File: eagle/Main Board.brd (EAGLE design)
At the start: 101.6 x 53.3 mm, 3 parts

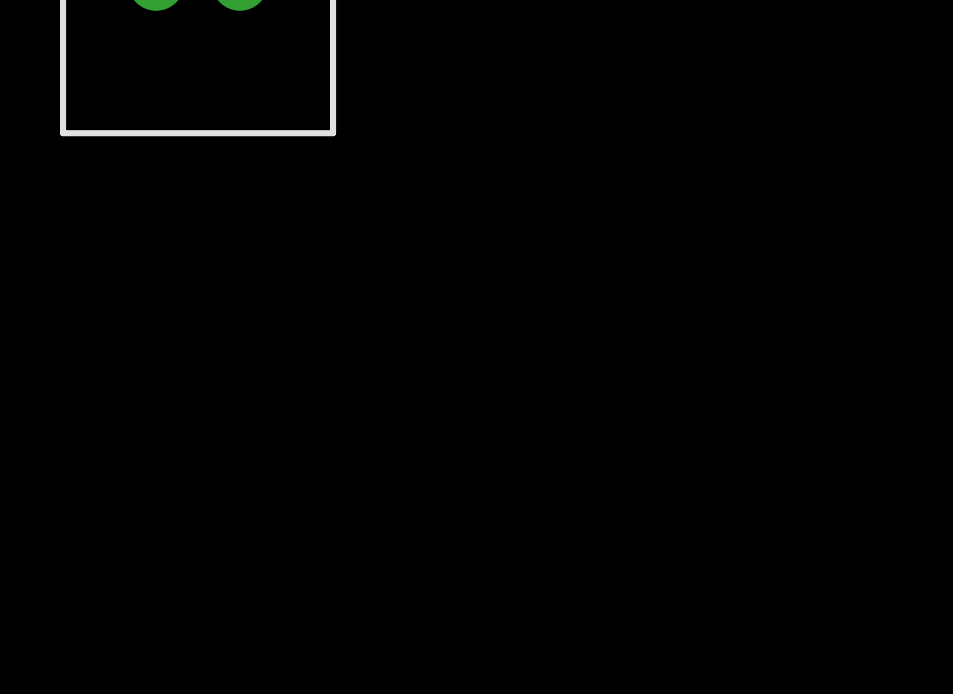
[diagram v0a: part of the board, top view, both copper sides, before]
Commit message: Wired rotary encoder to arduino.
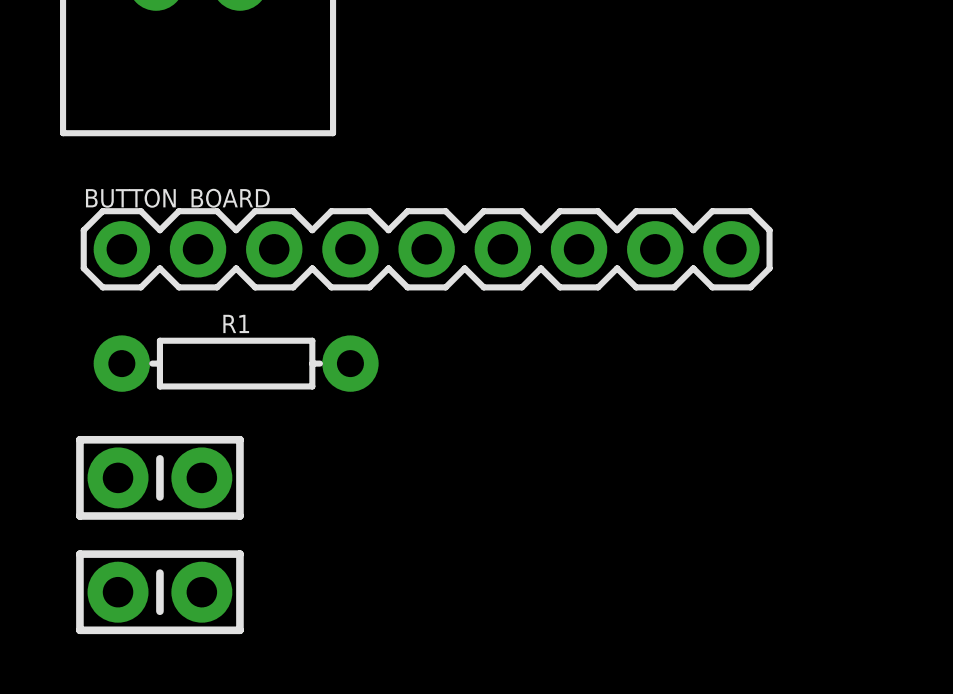
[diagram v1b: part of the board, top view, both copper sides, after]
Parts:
- added BUTTON_BOARD: (no value), SparkFun-Connectors:1X09
- added C1, C2: 0.1uF, SparkFun-Capacitors:CAP-PTH-SMALL-KIT
- added R1: 10k, SparkFun-Resistors:AXIAL-0.3
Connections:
- new net 5V: B1.5V, B1.5V@1, B1.5V@2, BUTTON_BOARD.1
- new net KEY: BUTTON_BOARD.3
- new net LED_B: B1.6, BUTTON_BOARD.9
- new net LED_G: B1.5, BUTTON_BOARD.8
- new net LED_R: B1.4, BUTTON_BOARD.7
- new net ROT_A: B1.2, BUTTON_BOARD.4, C1.2
- new net ROT_B: B1.7, BUTTON_BOARD.5, C2.2
- new net ROT_SW: B1.3, BUTTON_BOARD.6, R1.P$2
- net GND: now also B1.GND, B1.GND@1, B1.GND@2, B1.GND@3, B1.GND@4, BUTTON_BOARD.2, C1.1, C2.1, R1.P$1
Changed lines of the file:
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@@
 </element>
 <element name="J1" library="SparkFun-Connectors" package="2X8-SHROUDED_LOCK" value="" x="-106.68" y="12.7" smashed="yes"/>
+<element name="BUTTON_BOARD" library="SparkFun-Connectors" package="1X09" value="" x="-109.22" y="-5.08" smashed="yes">
+<attribute name="NAME" x="-110.49" y="-3.683" size="0.6096" layer="25" font="vector" ratio="20"/>
+<attribute name="VALUE" x="-110.49" y="-7.112" size="0.6096" layer="27" font="vector" ratio="20"/>
+</element>
+<element name="R1" library="SparkFun-Resistors" package="AXIAL-0.3" value="10k" x="-105.41" y="-8.89" smashed="yes">
+<attribute name="NAME" x="-105.41" y="-7.874" size="0.6096" layer="25" font="vector" ratio="20" align="bottom-center"/>
+<attribute name="PROD_ID" value="RES-12183" x="-105.41" y="-8.89" size="1.778" layer="27" display="off"/>
+<attribute name="VALUE" x="-105.41" y="-9.906" size="0.6096" layer="27" font="vector" ratio="20" align="top-center"/>
+</element>
+<element name="C1" library="SparkFun-Capacitors" package="CAP-PTH-SMALL-KIT" value="0.1uF" x="-107.95" y="-12.7" smashed="yes">
+<attribute name="PROD_ID" value="CAP-08370" x="-107.95" y="-12.7" size="1.778" layer="27" display="off"/>
+</element>
+<element name="C2" library="SparkFun-Capacitors" package="CAP-PTH-SMALL-KIT" value="0.1uF" x="-107.95" y="-16.51" smashed="yes">
+<attribute name="PROD_ID" value="CAP-08370" x="-107.95" y="-16.51" size="1.778" layer="27" display="off"/>
+</element>
 </elements>
 <signals>
@@
 <signal name="GND">
 <contactref element="J1" pad="4"/>
+<contactref element="B1" pad="GND@1"/>
+<contactref element="B1" pad="GND@3" route="any" routetag="B1.GND"/>
+<contactref element="B1" pad="GND@4" route="any" routetag="B1.GND"/>
+<contactref element="B1" pad="GND" route="any" routetag="B1.GND"/>
+<contactref element="C1" pad="1"/>
+<contactref element="C2" pad="1"/>
+<contactref element="BUTTON_BOARD" pad="2"/>
+<contactref element="B1" pad="GND@2"/>
+<contactref element="R1" pad="P$1"/>
+<wire x1="-109.347" y1="-12.7" x2="-109.347" y2="-16.51" width="0" layer="19" extent="1-1"/>
+<wire x1="-109.22" y1="-8.89" x2="-109.347" y2="-12.7" width="0" layer="19" extent="1-1"/>
+<wire x1="-106.68" y1="-5.08" x2="-109.22" y2="-8.89" width="0" layer="19" extent="1-1"/>
+<wire x1="-105.283" y1="19.05" x2="-106.68" y2="-5.08" width="0" layer="19" extent="1-1"/>
+<wire x1="26.67" y1="50.8" x2="-105.283" y2="19.05" width="0" layer="19" extent="1-1"/>
+<wire x1="93.98" y1="7.62" x2="96.52" y2="7.62" width="0" layer="19" extent="1-1"/>
+<wire x1="43.18" y1="2.54" x2="40.64" y2="2.54" width="0" layer="19" extent="1-1"/>
+</signal>
+<signal name="ROT_A">
+<contactref element="B1" pad="2"/>
+<contactref element="BUTTON_BOARD" pad="4"/>
+<contactref element="C1" pad="2"/>
+<wire x1="-101.6" y1="-5.08" x2="-106.553" y2="-12.7" width="0" layer="19" extent="1-1"/>
+<wire x1="58.42" y1="50.8" x2="-101.6" y2="-5.08" width="0" layer="19" extent="1-1"/>
+</signal>
+<signal name="5V">
+<contactref element="B1" pad="5V@2"/>
+<contactref element="B1" pad="5V@1"/>
+<contactref element="B1" pad="5V"/>
+<contactref element="BUTTON_BOARD" pad="1"/>
+<wire x1="93.98" y1="50.8" x2="96.52" y2="50.8" width="0" layer="19" extent="1-1"/>
+<wire x1="38.1" y1="2.54" x2="93.98" y2="50.8" width="0" layer="19" extent="1-1"/>
+<wire x1="-109.22" y1="-5.08" x2="38.1" y2="2.54" width="0" layer="19" extent="1-1"/>
+</signal>
+<signal name="ROT_SW">
+<contactref element="B1" pad="3"/>
+<contactref element="BUTTON_BOARD" pad="6"/>
+<contactref element="R1" pad="P$2"/>
+<wire x1="-96.52" y1="-5.08" x2="-101.6" y2="-8.89" width="0" layer="19" extent="1-1"/>
+<wire x1="55.88" y1="50.8" x2="-96.52" y2="-5.08" width="0" layer="19" extent="1-1"/>
+</signal>
+<signal name="LED_R">
+<contactref element="B1" pad="4"/>
+<contactref element="BUTTON_BOARD" pad="7"/>
+<wire x1="-93.98" y1="-5.08" x2="53.34" y2="50.8" width="0" layer="19" extent="1-1"/>
+</signal>
+<signal name="LED_G">
+<contactref element="B1" pad="5"/>
+<contactref element="BUTTON_BOARD" pad="8"/>
+<wire x1="-91.44" y1="-5.08" x2="50.8" y2="50.8" width="0" layer="19" extent="1-1"/>
+</signal>
+<signal name="LED_B">
+<contactref element="B1" pad="6"/>
+<contactref element="BUTTON_BOARD" pad="9"/>
+<wire x1="-88.9" y1="-5.08" x2="48.26" y2="50.8" width="0" layer="19" extent="1-1"/>
+</signal>
+<signal name="ROT_B">
+<contactref element="B1" pad="7"/>
+<contactref element="BUTTON_BOARD" pad="5"/>
+<contactref element="C2" pad="2"/>
+<wire x1="-99.06" y1="-5.08" x2="-106.553" y2="-16.51" width="0" layer="19" extent="1-1"/>
+<wire x1="45.72" y1="50.8" x2="-99.06" y2="-5.08" width="0" layer="19" extent="1-1"/>
+</signal>
+<signal name="KEY">
+<contactref element="BUTTON_BOARD" pad="3"/>
 </signal>
 </signals>
